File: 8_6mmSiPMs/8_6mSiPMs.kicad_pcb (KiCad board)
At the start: 2 copper layers, 52.7 x 25.4 mm, 18 parts

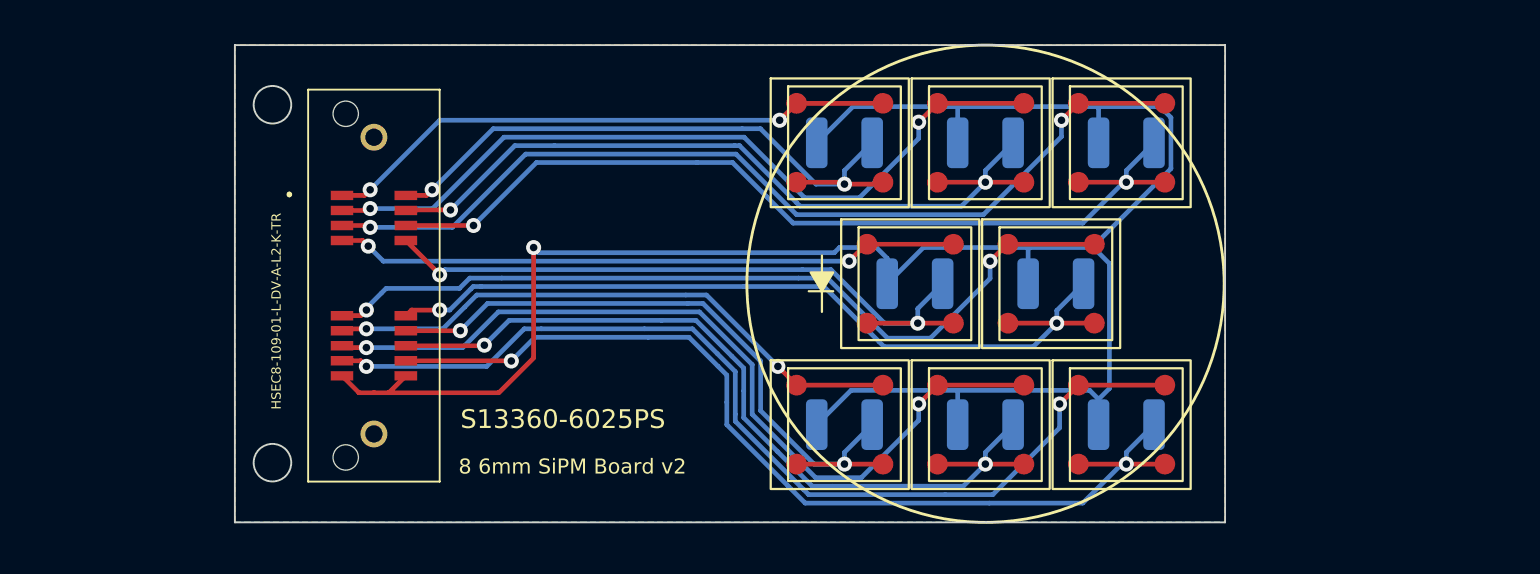
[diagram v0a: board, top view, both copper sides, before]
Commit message: Updated PCBs to include temp sensors
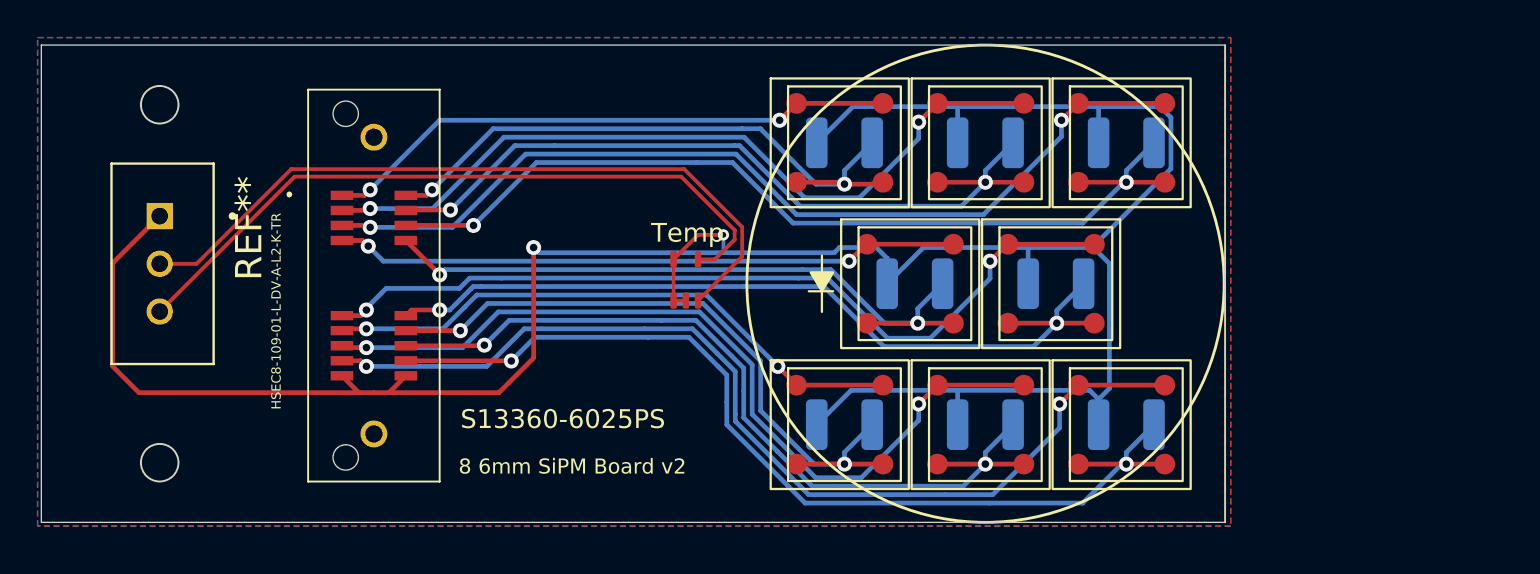
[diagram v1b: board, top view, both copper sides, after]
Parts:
- added REF**: TE_103414-1, AMPMODU:TE_103414-1, F.Cu at (115.0, 106.5)
- added Temp: LM94021QBIMG-NOPB, Sensor:LM94021QBIMG-NOPB, F.Cu at (143.0, 107.4)
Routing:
- net TMP_OUT: track 0.00 -> 39.3 mm
- net TMP_VDD: track 0.00 -> 37.6 mm
- net GND: track 113.1 -> 142.9 mm, vias 1 -> 2
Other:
- board size 52.7 x 25.4 mm -> 63 x 25.4 mm

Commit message: Updated boards with connector HSEC8-109-01-L-DV-A-BL
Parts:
- removed the REF**10 at (166.4, 100.1)
- removed the REF**10 at (158.9, 100.1)
- removed the REF**10 at (151.4, 100.1)
- removed the REF**10 at (162.7, 107.6)
- removed the REF**10 at (155.2, 107.6)
- added REF**: Hamamatsu_S14160-6050HS, OptoDevice:Hamamatsu_S14160-6050HS, F.Cu at (183.0, 116.0)
- added REF**: Hamamatsu_S14160-6050HS, OptoDevice:Hamamatsu_S14160-6050HS, F.Cu at (151.5, 100.0)
- added REF**: Hamamatsu_S14160-6050HS, OptoDevice:Hamamatsu_S14160-6050HS, F.Cu at (162.0, 107.5)
- added REF**: Hamamatsu_S14160-6050HS, OptoDevice:Hamamatsu_S14160-6050HS, F.Cu at (158.5, 100.0)
- added REF**: Hamamatsu_S14160-6050HS, OptoDevice:Hamamatsu_S14160-6050HS, F.Cu at (155.0, 107.5)
- added REF**: Hamamatsu_S14160-6050HS, OptoDevice:Hamamatsu_S14160-6050HS, F.Cu at (165.5, 100.0)
- moved 10 nF 0.95 mm to (165.5, 100.0)
- moved 10 nF 0.70 mm to (162.0, 107.5)
- moved 10 nF 0.45 mm to (158.5, 100.0)
- moved 10 nF 0.22 mm to (155.0, 107.5)
- moved 10 nF 0.12 mm to (151.5, 100.0)
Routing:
- net GND: track 142.9 -> 58.5 mm
- net 2A: track 49.3 -> 18.8 mm, vias 2 -> 1
- net 2C: track 49.7 -> 22.6 mm, vias 2 -> 1
- net 1A: track 41.4 -> 19.2 mm, vias 2 -> 1
- net 4A: track 44.4 -> 22.9 mm, vias 2 -> 1
- net 1C: track 41.9 -> 23.0 mm, vias 2 -> 1
- net 4C: track 44.9 -> 26.7 mm, vias 2 -> 1
- net 0A: track 33.8 -> 20.3 mm, vias 2 -> 1
- net 3A: track 36.6 -> 23.5 mm, vias 2 -> 1
- net 3C: track 33.4 -> 27.4 mm, vias 2 -> 1
- net 0C: track 30.8 -> 25.0 mm, vias 2 -> 1
- removed copper zone on B.Cu, net (none)
- removed copper zone on F.Cu, net (none)
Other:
- board text added: "8 6mm SiPM Board v3"
- board text added: "Hamamatsu_S14160-6050HS"
- board text removed: "8 6mm SiPM Board v2"
- board text removed: "S13360-6025PS"
